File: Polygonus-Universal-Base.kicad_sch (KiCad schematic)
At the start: 11 parts, among them J1 Conn_02x04_Top_Bottom, J4 Polygonus_Plugs, J5 Conn_02x04_Top_Bottom, U1 WBO-Single-Module, U14 WBO-Single-Module

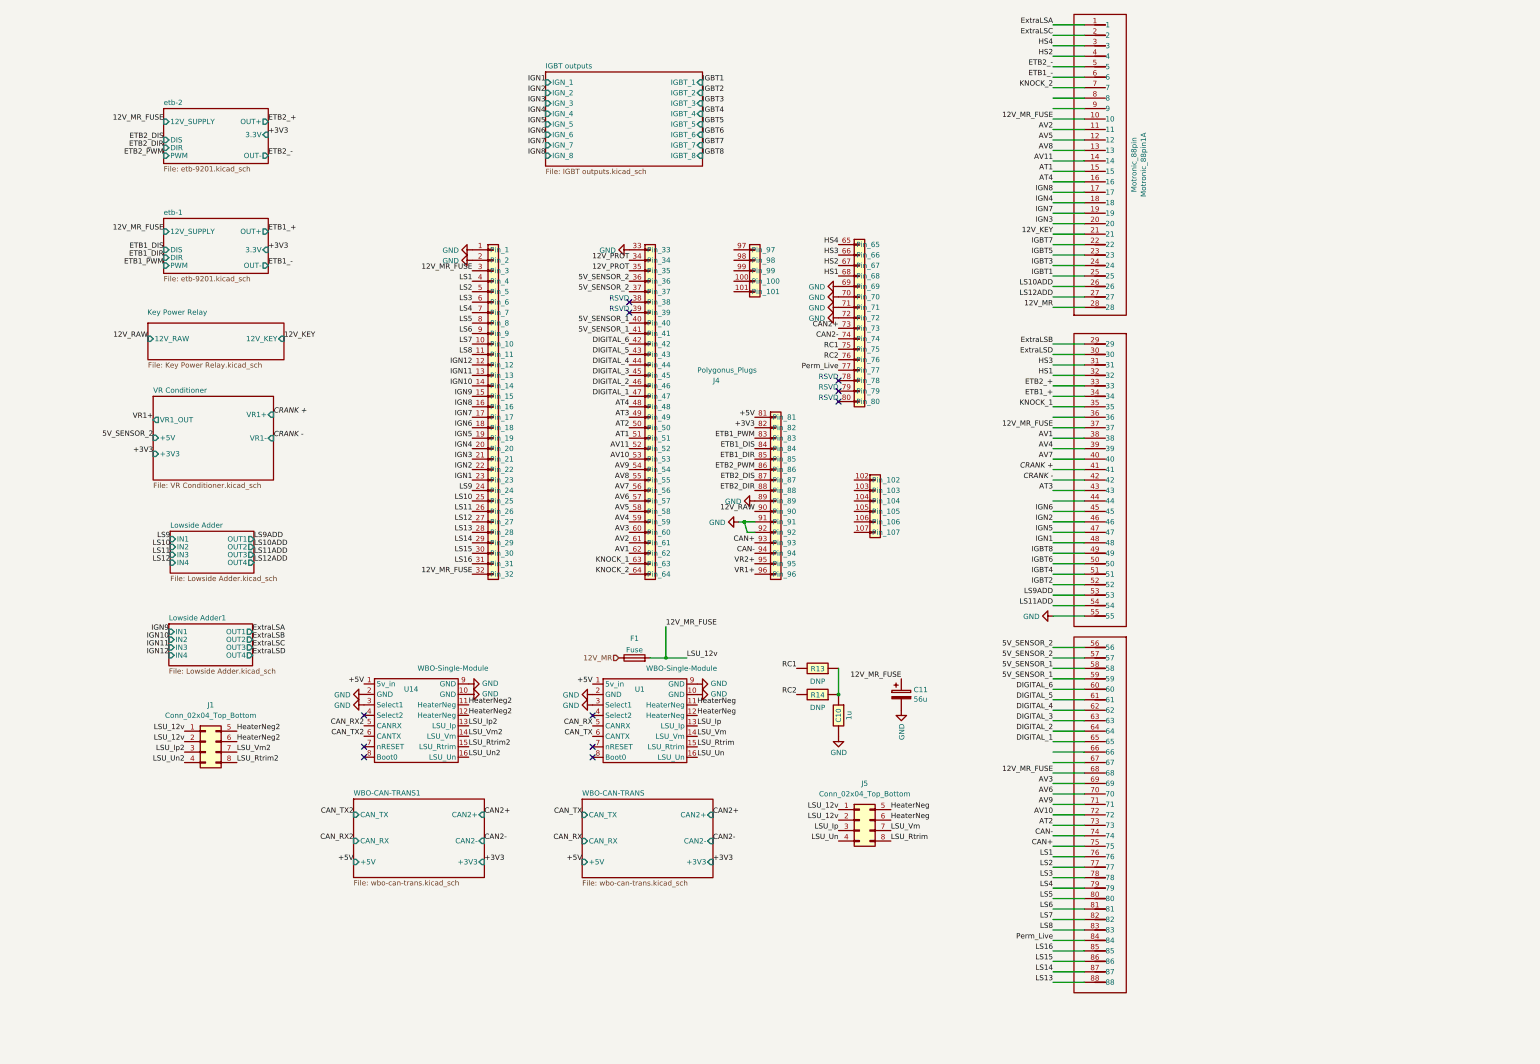
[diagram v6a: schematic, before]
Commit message: Fixed 12V_RAW and added grounds for sensors
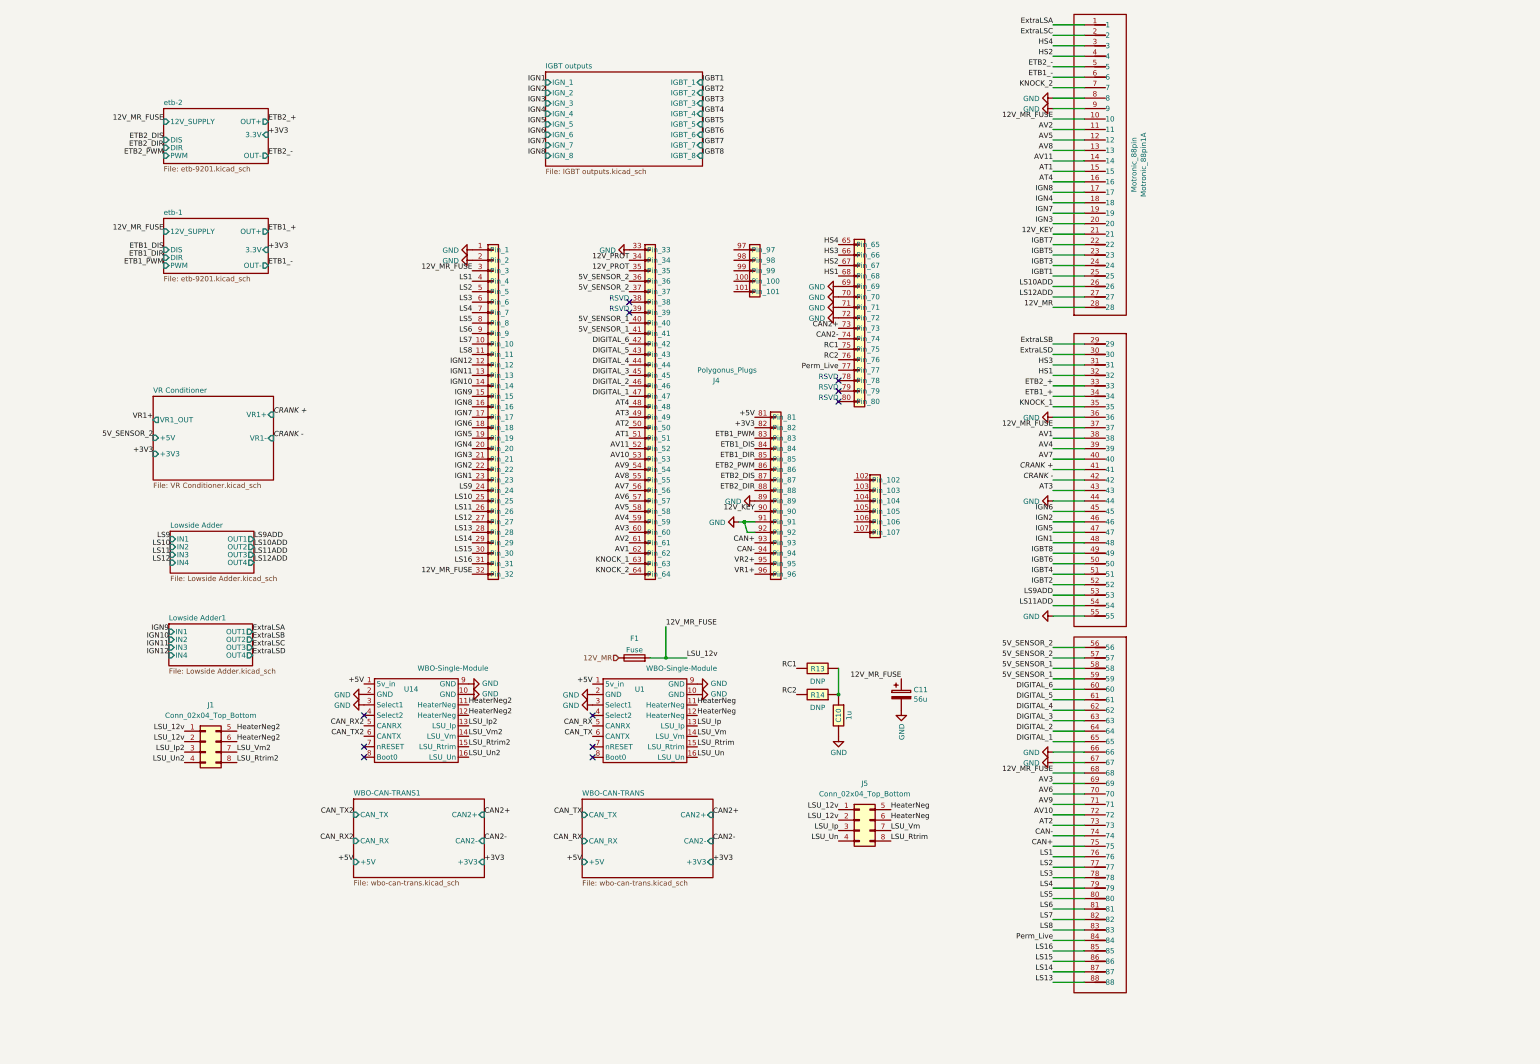
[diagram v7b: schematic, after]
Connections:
- net 12V_RAW is gone; now on net 12V_KEY: J4.90 (Pin_90)
- net GND: now also Motronic_88pin1.36, Motronic_88pin1.44, Motronic_88pin1.66, Motronic_88pin1.67, Motronic_88pin1.8, Motronic_88pin1.9
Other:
- removed sheet Key Power Relay
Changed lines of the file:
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@@
     (effects (font (size 1.27 1.27)) (justify right bottom))
   )
-  (label "12V_RAW" (at 199.39 148.59 180)
+  (label "12V_KEY" (at 199.39 148.59 180)
     (effects (font (size 1.27 1.27)) (justify right bottom))
   )
@@
     (effects (font (size 1.27 1.27)) (justify right bottom))
   )
-  (label "12V_RAW" (at 52.07 106.68 180)
-    (effects (font (size 1.27 1.27)) (justify right bottom))
-  )
   (label "KNOCK_2" (at 168.91 163.83 180)
     (effects (font (size 1.27 1.27)) (justify right bottom))
@@
   (label "IGN6" (at 148.59 57.15 180)
     (effects (font (size 1.27 1.27)) (justify right bottom))
-  )
-  (label "12V_KEY" (at 85.09 106.68 0)
-    (effects (font (size 1.27 1.27)) (justify left bottom))
   )
   (label "AV1" (at 168.91 158.75 180)
@@
     )
     (property "Datasheet" "" (id 3) (at 195.5294 151.1603 0)
+      (effects (font (size 1.27 1.27)) hide)
+    )
+    (pin "1")
+  )
+  (symbol (lib_id "power:GND") (at 271.78 146.05 270) (unit 1)
+    (in_bom yes) (on_board yes)
+    (property "Reference" "#PWR?" (id 0) (at 265.43 146.05 0)
+      (effects (font (size 1.27 1.27)) hide)
+    )
+    (property "Value" "GND" (id 1) (at 268.5288 146.177 90)
+      (effects (font (size 1.27 1.27)) (justify right))
+    )
+    (property "Footprint" "" (id 2) (at 271.78 146.05 0)
+      (effects (font (size 1.27 1.27)) hide)
+    )
+    (property "Datasheet" "" (id 3) (at 271.78 146.05 0)
       (effects (font (size 1.27 1.27)) hide)
     )
@@
     (pin "9")
   )
+  (symbol (lib_id "power:GND") (at 271.78 48.26 270) (unit 1)
+    (in_bom yes) (on_board yes)
+    (property "Reference" "#PWR?" (id 0) (at 265.43 48.26 0)
+      (effects (font (size 1.27 1.27)) hide)
+    )
+    (property "Value" "GND" (id 1) (at 268.5288 48.387 90)
+      (effects (font (size 1.27 1.27)) (justify right))
+    )
+    (property "Footprint" "" (id 2) (at 271.78 48.26 0)
+      (effects (font (size 1.27 1.27)) hide)
+    )
+    (property "Datasheet" "" (id 3) (at 271.78 48.26 0)
+      (effects (font (size 1.27 1.27)) hide)
+    )
+    (pin "1")
+  )
   (symbol (lib_id "Simon:WBO-Single-Module") (at 171.45 193.04 0) (unit 1)
     (in_bom yes) (on_board yes)
@@
     (pin "1")
   )
+  (symbol (lib_id "power:GND") (at 271.78 207.01 270) (unit 1)
+    (in_bom yes) (on_board yes)
+    (property "Reference" "#PWR?" (id 0) (at 265.43 207.01 0)
+      (effects (font (size 1.27 1.27)) hide)
+    )
+    (property "Value" "GND" (id 1) (at 268.5288 207.137 90)
+      (effects (font (size 1.27 1.27)) (justify right))
+    )
+    (property "Footprint" "" (id 2) (at 271.78 207.01 0)
+      (effects (font (size 1.27 1.27)) hide)
+    )
+    (property "Datasheet" "" (id 3) (at 271.78 207.01 0)
+      (effects (font (size 1.27 1.27)) hide)
+    )
+    (pin "1")
+  )
   (symbol (lib_id "hellen-one-common:Res") (at 219.71 193.04 90) (mirror x) (unit 1)
     (in_bom yes) (on_board yes)
@@
     )
     (property "Datasheet" "" (id 3) (at 185.42 190.5 0)
+      (effects (font (size 1.27 1.27)) hide)
+    )
+    (pin "1")
+  )
+  (symbol (lib_id "power:GND") (at 271.78 50.8 270) (unit 1)
+    (in_bom yes) (on_board yes)
+    (property "Reference" "#PWR?" (id 0) (at 265.43 50.8 0)
+      (effects (font (size 1.27 1.27)) hide)
+    )
+    (property "Value" "GND" (id 1) (at 268.5288 50.927 90)
+      (effects (font (size 1.27 1.27)) (justify right))
+    )
+    (property "Footprint" "" (id 2) (at 271.78 50.8 0)
+      (effects (font (size 1.27 1.27)) hide)
+    )
+    (property "Datasheet" "" (id 3) (at 271.78 50.8 0)
+      (effects (font (size 1.27 1.27)) hide)
+    )
+    (pin "1")
+  )
+  (symbol (lib_id "power:GND") (at 271.78 209.55 270) (unit 1)
+    (in_bom yes) (on_board yes)
+    (property "Reference" "#PWR?" (id 0) (at 265.43 209.55 0)
+      (effects (font (size 1.27 1.27)) hide)
+    )
+    (property "Value" "GND" (id 1) (at 268.5288 209.677 90)
+      (effects (font (size 1.27 1.27)) (justify right))
+    )
+    (property "Footprint" "" (id 2) (at 271.78 209.55 0)
+      (effects (font (size 1.27 1.27)) hide)
+    )
+    (property "Datasheet" "" (id 3) (at 271.78 209.55 0)
       (effects (font (size 1.27 1.27)) hide)
     )
@@
     (pin "2")
   )
+  (symbol (lib_id "power:GND") (at 271.78 125.73 270) (unit 1)
+    (in_bom yes) (on_board yes)
+    (property "Reference" "#PWR?" (id 0) (at 265.43 125.73 0)
+      (effects (font (size 1.27 1.27)) hide)
+    )
+    (property "Value" "GND" (id 1) (at 268.5288 125.857 90)
+      (effects (font (size 1.27 1.27)) (justify right))
+    )
+    (property "Footprint" "" (id 2) (at 271.78 125.73 0)
+      (effects (font (size 1.27 1.27)) hide)
+    )
+    (property "Datasheet" "" (id 3) (at 271.78 125.73 0)
+      (effects (font (size 1.27 1.27)) hide)
+    )
+    (pin "1")
+  )
   (symbol (lib_id "power:GND") (at 129.927 193.0073 90) (unit 1)
     (in_bom yes) (on_board yes)
@@
     )
   )
-  (sheet (at 52.07 102.87) (size 33.02 8.89)
-    (stroke (width 0.1524) (type solid) (color 0 0 0 0))
-    (fill (color 0 0 0 0.0000))
-    (property "Sheet name" "Key Power Relay" (id 0) (at 51.9202 100.9872 0)
-      (effects (font (size 1.27 1.27)) (justify left bottom))
-    )
-    (property "Sheet file" "Key Power Relay.kicad_sch" (id 1) (at 52.07 112.3446 0)
-      (effects (font (size 1.27 1.27)) (justify left top))
-    )
-    (pin "12V_KEY" input (at 85.09 106.68 0)
-      (effects (font (size 1.27 1.27)) (justify right))
-    )
-    (pin "12V_RAW" input (at 52.07 106.68 180)
-      (effects (font (size 1.27 1.27)) (justify left))
-    )
-  )
   (sheet (at 57.4793 153.4054) (size 20.32 10.16) (fields_autoplaced)
     (stroke (width 0) (type solid) (color 0 0 0 0))
@@
     (path "/" (page "1"))
     (path "/eb1c8308-a44a-4a4b-a646-1cfc69b467a3" (page "2"))
-    (path "/c3092a4f-f5c4-4859-a4ac-211b2ff8bb43" (page "3"))
     (path "/76f66c7e-94ea-4f9a-aa2e-a01725934e38" (page "4"))
     (path "/39654894-3080-4f33-9285-6e0d77694cfd" (page "5"))
@@
       (reference "#PWR0125") (unit 1) (value "GND") (footprint "")
     )
+    (path "/16b8e6ae-f2bd-4055-8ee5-118ea183bedc"
+      (reference "#PWR?") (unit 1) (value "GND") (footprint "")
+    )
+    (path "/1e43e114-9fc6-46c3-bb21-fb9a05ca3f90"
+      (reference "#PWR?") (unit 1) (value "GND") (footprint "")
+    )
+    (path "/3fca0492-260c-4cb6-944d-0b2f5185c032"
+      (reference "#PWR?") (unit 1) (value "GND") (footprint "")
+    )
+    (path "/4704ec4c-39bb-4e09-a18d-b3d1688e0d90"
+      (reference "#PWR?") (unit 1) (value "GND") (footprint "")
+    )
+    (path "/572ddfc6-7632-42f3-a20f-3c35a0a51e19"
+      (reference "#PWR?") (unit 1) (value "GND") (footprint "")
+    )
+    (path "/d59e300e-de29-450d-a1d3-0d56255d0dcb"
+      (reference "#PWR?") (unit 1) (value "GND") (footprint "")
+    )
     (path "/eb1c8308-a44a-4a4b-a646-1cfc69b467a3/f24afa40-97ba-4ecd-beec-81539bdccf6b"

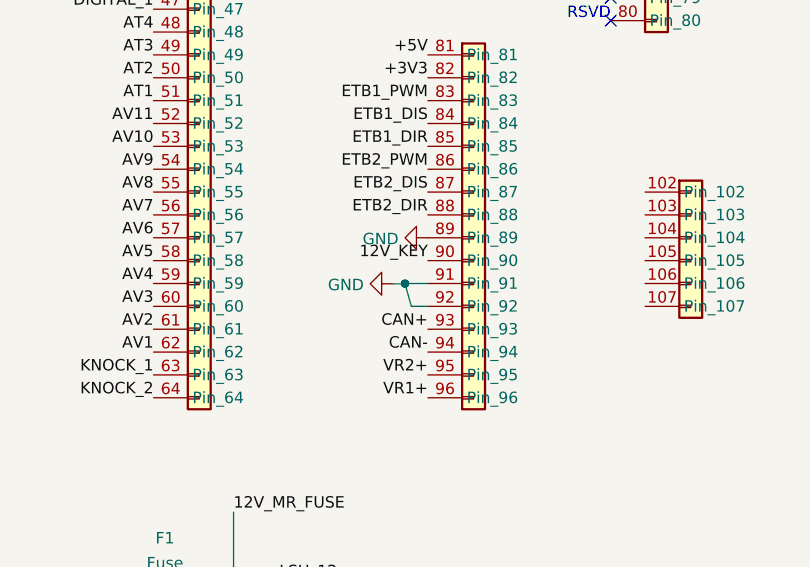
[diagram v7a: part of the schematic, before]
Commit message: convert to kicad7, add jumpers for direct drive igbt output
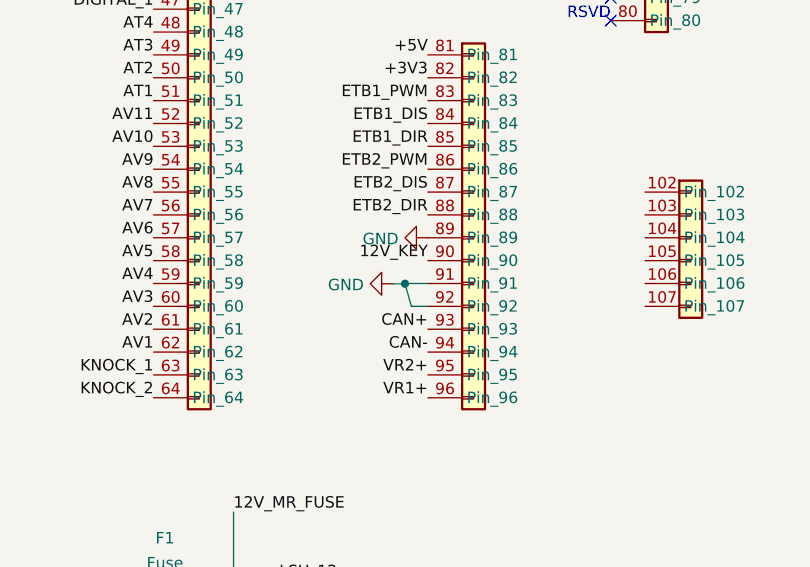
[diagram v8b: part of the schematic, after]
